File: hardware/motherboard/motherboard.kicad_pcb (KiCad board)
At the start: 6 copper layers, 32.4 x 32 mm, 2 parts, among them U201 STM32MP157AACx, U401 K4E6E304ED-EGCG

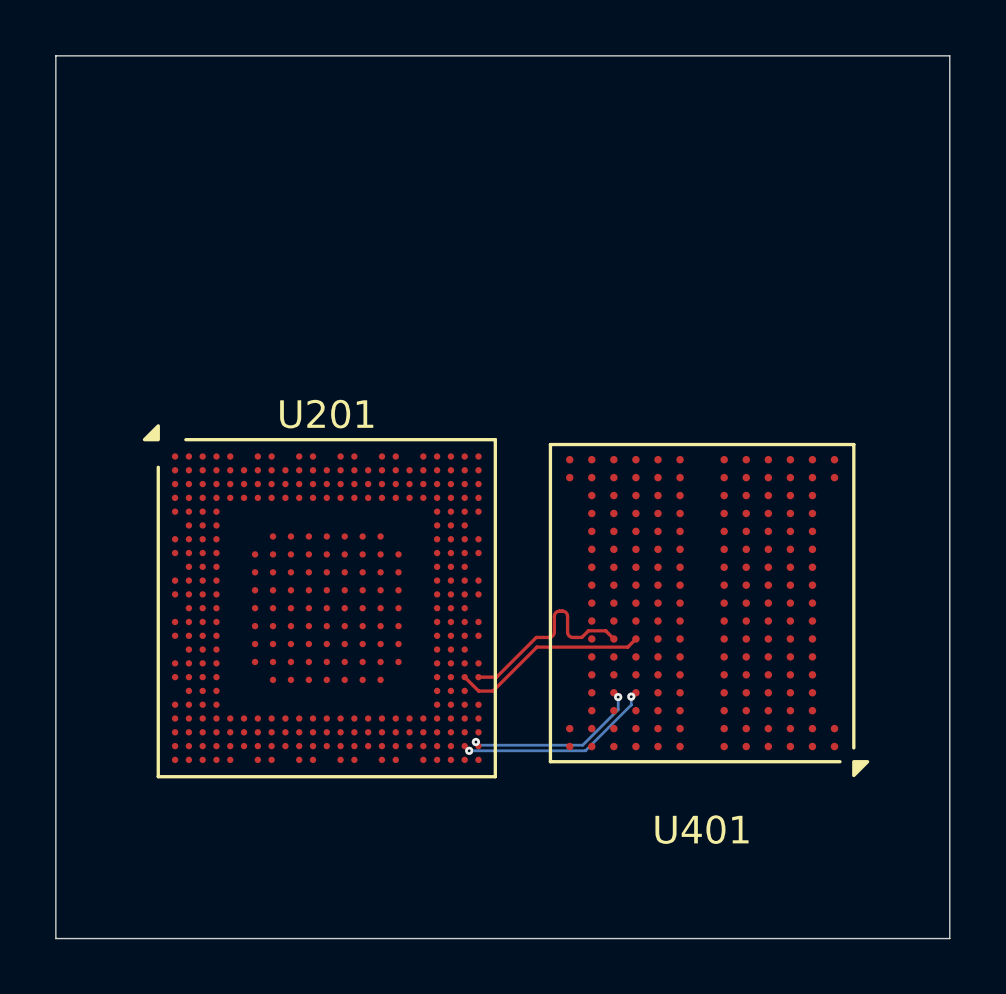
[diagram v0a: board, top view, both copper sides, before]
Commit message: Start routing RAM, add more docs
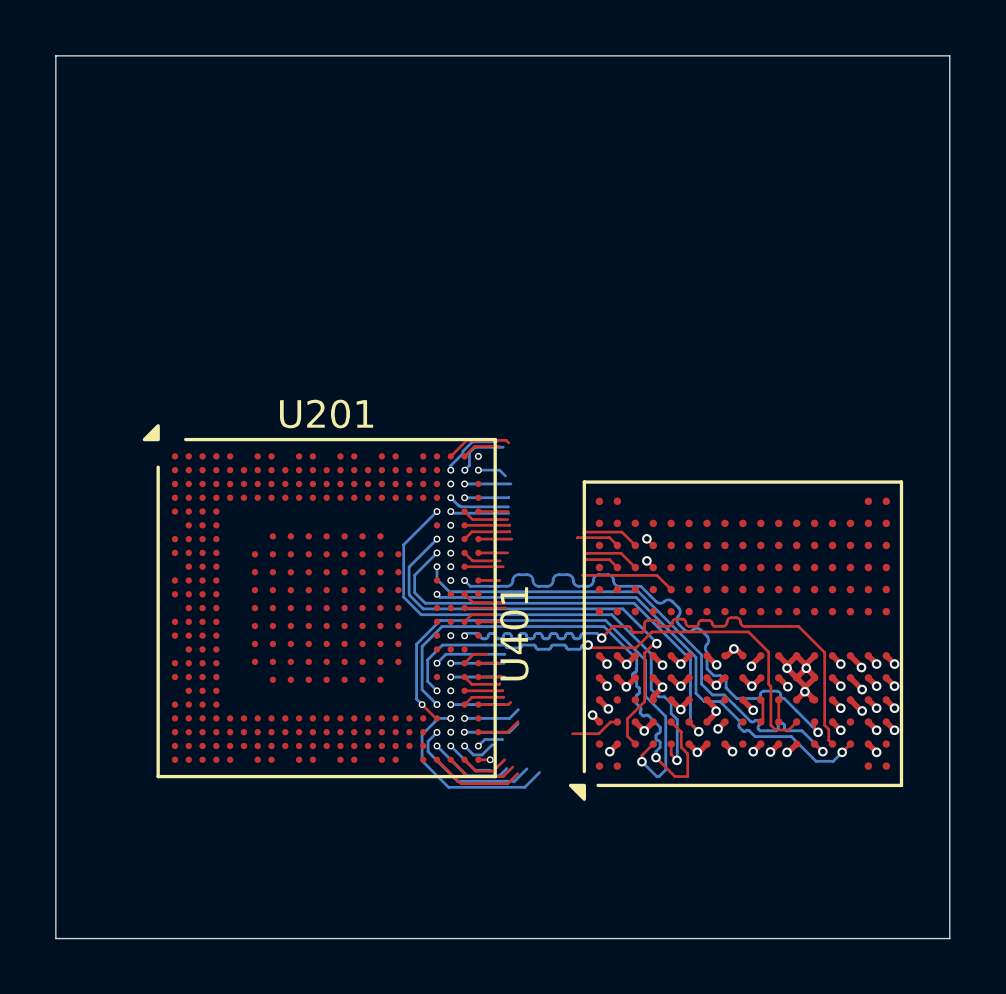
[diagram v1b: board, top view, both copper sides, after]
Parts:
- moved U401 1.85 mm to (151.3, 87.5), turned to 90 degrees
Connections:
- U401 pad A10: /RAM/VDD1 -> /CPU/PWR.VDD_{DDR}
- U401 pad A11: /RAM/VDDQ -> /CPU/PWR.VDD_{DDR}
- U401 pad A3: /RAM/VDD1 -> /CPU/PWR.VDD_{DDR}
- U401 pad A4: /RAM/VDD1 -> /CPU/PWR.VDD_{DDR}
- U401 pad A5: /RAM/VDD1 -> /CPU/PWR.VDD_{DDR}
- U401 pad A6: /RAM/VDD1 -> /CPU/PWR.VDD_{DDR}
- U401 pad A8: /RAM/VDD2 -> /CPU/PWR.VDD_{DDR}
- U401 pad A9: /RAM/VDD2 -> /CPU/PWR.VDD_{DDR}
- U401 pad C12: /RAM/VDDQ -> /CPU/PWR.VDD_{DDR}
- U401 pad D4: /RAM/VDD2 -> /CPU/PWR.VDD_{DDR}
- U401 pad D5: /RAM/VDD2 -> /CPU/PWR.VDD_{DDR}
- U401 pad D6: /RAM/VDD2 -> /CPU/PWR.VDD_{DDR}
- U401 pad E12: /RAM/VDDQ -> /CPU/PWR.VDD_{DDR}
- U401 pad E8: /RAM/VDDQ -> /CPU/PWR.VDD_{DDR}
- U401 pad F2: /RAM/VDDCA -> /CPU/PWR.VDD_{DDR}
- U401 pad G12: /RAM/VDDQ -> /CPU/PWR.VDD_{DDR}
- U401 pad G2: /RAM/VDDCA -> /CPU/PWR.VDD_{DDR}
- U401 pad G5: /RAM/VDD2 -> /CPU/PWR.VDD_{DDR}
- U401 pad H11: /RAM/VDDQ -> /CPU/PWR.VDD_{DDR}
- U401 pad H12: /RAM/VDD2 -> /CPU/PWR.VDD_{DDR}
- U401 pad H3: /RAM/VDDCA -> /CPU/PWR.VDD_{DDR}
- U401 pad H5: /RAM/VDD2 -> /CPU/PWR.VDD_{DDR}
- U401 pad H6: /RAM/VDD2 -> /CPU/PWR.VDD_{DDR}
- U401 pad H8: /RAM/VDDQ -> /CPU/PWR.VDD_{DDR}
- U401 pad H9: /RAM/VDDQ -> /CPU/PWR.VDD_{DDR}
- U401 pad J10: /RAM/VDDQ -> /CPU/PWR.VDD_{DDR}
- U401 pad J5: /RAM/VDD2 -> /CPU/PWR.VDD_{DDR}
- U401 pad J6: /RAM/VDD2 -> /CPU/PWR.VDD_{DDR}
- U401 pad J9: /RAM/VDDQ -> /CPU/PWR.VDD_{DDR}
- U401 pad K11: /RAM/VDDQ -> /CPU/PWR.VDD_{DDR}
- U401 pad K12: /RAM/VDD2 -> /CPU/PWR.VDD_{DDR}
- U401 pad K5: /RAM/VDD2 -> /CPU/PWR.VDD_{DDR}
- U401 pad K6: /RAM/VDD2 -> /CPU/PWR.VDD_{DDR}
- U401 pad K8: /RAM/VDDQ -> /CPU/PWR.VDD_{DDR}
- U401 pad L12: /RAM/VDDQ -> /CPU/PWR.VDD_{DDR}
- U401 pad L2: /RAM/VDDCA -> /CPU/PWR.VDD_{DDR}
- U401 pad L5: /RAM/VDD2 -> /CPU/PWR.VDD_{DDR}
- U401 pad M2: /RAM/VDDCA -> /CPU/PWR.VDD_{DDR}
- U401 pad N12: /RAM/VDDQ -> /CPU/PWR.VDD_{DDR}
- U401 pad N8: /RAM/VDDQ -> /CPU/PWR.VDD_{DDR}
- U401 pad P4: /RAM/VDD2 -> /CPU/PWR.VDD_{DDR}
- U401 pad P5: /RAM/VDD2 -> /CPU/PWR.VDD_{DDR}
- U401 pad P6: /RAM/VDD2 -> /CPU/PWR.VDD_{DDR}
- U401 pad R12: /RAM/VDDQ -> /CPU/PWR.VDD_{DDR}
- U401 pad U10: /RAM/VDD1 -> /CPU/PWR.VDD_{DDR}
- U401 pad U11: /RAM/VDDQ -> /CPU/PWR.VDD_{DDR}
- U401 pad U3: /RAM/VDD1 -> /CPU/PWR.VDD_{DDR}
- U401 pad U4: /RAM/VDD1 -> /CPU/PWR.VDD_{DDR}
- U401 pad U5: /RAM/VDD1 -> /CPU/PWR.VDD_{DDR}
- U401 pad U6: /RAM/VDD1 -> /CPU/PWR.VDD_{DDR}
- U401 pad U8: /RAM/VDD2 -> /CPU/PWR.VDD_{DDR}
- U401 pad U9: /RAM/VDD2 -> /CPU/PWR.VDD_{DDR}
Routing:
- net /CPU/DDR.A1: track 0.00 -> 20.1 mm, vias 0 -> 2
- net GND: track 0.00 -> 19.6 mm, vias 0 -> 32
- net /CPU/DDR.A6: track 0.00 -> 19.1 mm, vias 0 -> 2
- net /CPU/DDR.A0: track 0.00 -> 18.7 mm, vias 0 -> 2
- net /CPU/DDR.A2: track 0.00 -> 18.7 mm, vias 0 -> 2
- net /CPU/DDR.A4: track 0.00 -> 18.7 mm, vias 0 -> 2
- net /CPU/DDR.A8: track 0.00 -> 18.5 mm, vias 0 -> 2
- net /CPU/DDR.A3: track 0.00 -> 18.5 mm, vias 0 -> 2
- net /CPU/DDR.A7: track 0.00 -> 18.5 mm, vias 0 -> 2
- net /CPU/DDR.A9: track 0.00 -> 16.4 mm, vias 0 -> 2
- net /CPU/DDR.A5: track 0.00 -> 16.0 mm, vias 0 -> 2
- net /CPU/PWR.VDD_{DDR}: track 0.00 -> 11.9 mm, vias 0 -> 22
- net /CPU/DDR.DQ15: track 0.00 -> 7.12 mm, vias 0 -> 1
- net /CPU/DDR.DQS1-: track 7.28 -> 0.83 mm
- net /CPU/DDR.DQS1+: track 7.20 -> 1.40 mm
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- added copper zone on In2.Cu, net /CPU/PWR.VDD_{DDR}
- added copper zone on In1.Cu, net GND
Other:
- copper layers 6 -> 4

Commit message: Keep routing RAM
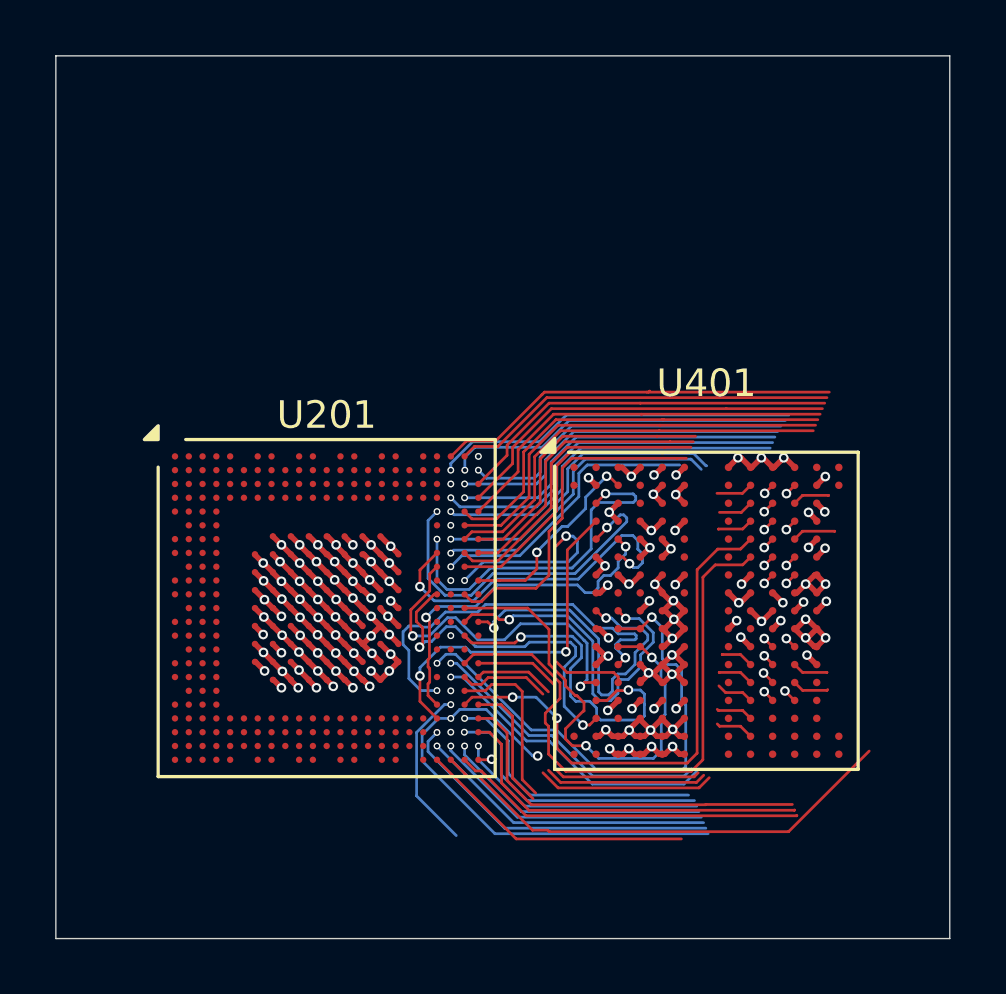
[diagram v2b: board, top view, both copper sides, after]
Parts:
- moved U401 1.56 mm to (150.0, 86.7), turned to 0 degrees
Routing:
- net GND: track 19.6 -> 55.6 mm, vias 32 -> 70
- net /CPU/PWR.VDD_{DDR}: track 11.9 -> 35.4 mm, vias 22 -> 38
- net /CPU/DDR.DQ10: track 0.96 -> 21.6 mm
- net /CPU/PWR.VDD_{CORE}: track 0.00 -> 15.2 mm, vias 0 -> 18
- net /CPU/DDR.CKE: track 3.45 -> 18.4 mm, vias 1 -> 2
- net /CPU/DDR.DQ0: track 1.68 -> 16.7 mm
- net /CPU/DDR.~{CS}: track 2.31 -> 17.1 mm, vias 0 -> 2
- net /CPU/DDR.DQ1: track 1.64 -> 16.4 mm
- net /CPU/DDR.DQ21: track 1.08 -> 15.7 mm
- net /CPU/DDR.DQ14: track 4.96 -> 19.4 mm, vias 0 -> 2
- net /CPU/DDR.DQ18: track 0.00 -> 14.2 mm
- net /CPU/DDR.DQ29: track 3.88 -> 17.9 mm, vias 0 -> 1
- net /CPU/DDR.DQM2: track 0.00 -> 14.0 mm
- net /CPU/DDR.DQS0+: track 1.75 -> 15.6 mm, vias 0 -> 1
- net /CPU/DDR.DQ30: track 1.60 -> 14.8 mm
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
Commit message: Rotate RAM IC, route data lanes partially
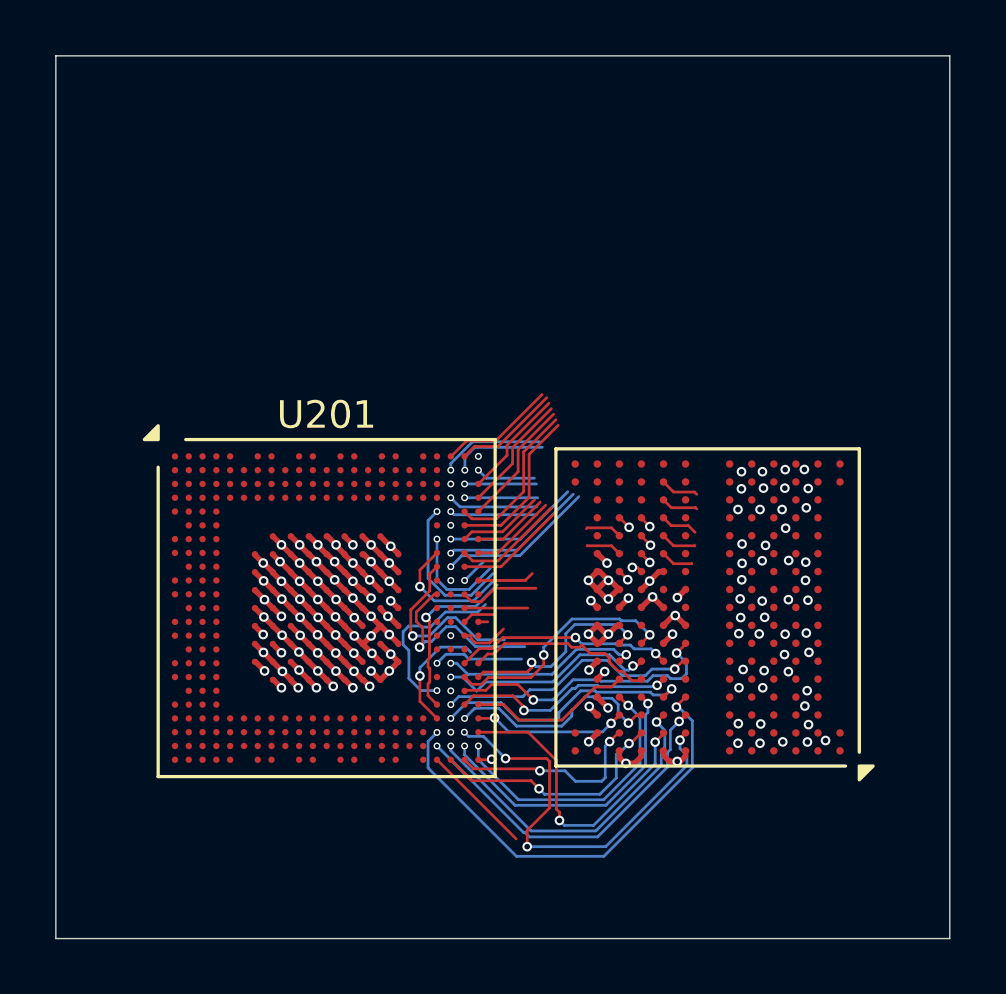
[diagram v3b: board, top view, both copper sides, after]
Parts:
- moved U401 0.13 mm to (150.0, 86.5), turned to 180 degrees
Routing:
- net GND: track 55.6 -> 33.5 mm, vias 70 -> 68
- net /CPU/PWR.VDD_{DDR}: track 35.4 -> 18.5 mm, vias 38 -> 37
- net /CPU/DDR.CKE: track 18.4 -> 3.27 mm
- net /CPU/DDR.~{CS}: track 17.1 -> 2.29 mm, vias 2 -> 1
- net /CPU/DDR.DQ10: track 21.6 -> 7.95 mm, vias 0 -> 2
- net /CPU/DDR.CLKN: track 12.8 -> 0.34 mm, vias 2 -> 1
- net /CPU/DDR.DQS0+: track 15.6 -> 3.53 mm
- net /CPU/DDR.A3: track 12.9 -> 0.95 mm, vias 2 -> 1
- net /CPU/DDR.CLKP: track 12.8 -> 1.18 mm, vias 2 -> 1
- net /CPU/DDR.DQ14: track 19.4 -> 8.15 mm
- net /CPU/DDR.A1: track 12.6 -> 1.79 mm, vias 2 -> 1
- net /CPU/DDR.DQ20: track 14.7 -> 4.24 mm
- net /CPU/DDR.DQ23: track 14.0 -> 3.86 mm
- net /CPU/DDR.DQS2-: track 12.7 -> 2.65 mm
- net /CPU/DDR.DQ22: track 13.2 -> 3.25 mm
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
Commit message: Add lpddr3 pcb layout rules, keep routing
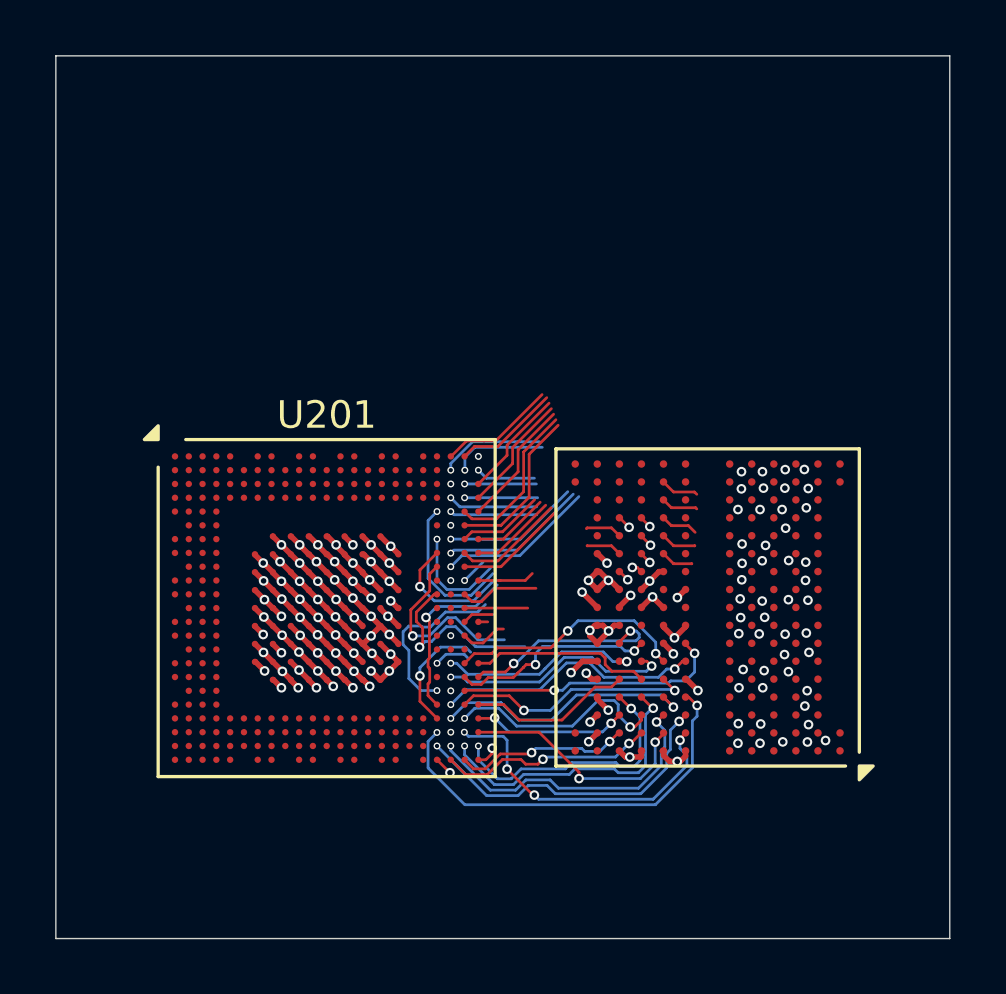
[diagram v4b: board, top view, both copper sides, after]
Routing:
- net /CPU/DDR.DQ31: track 15.3 -> 11.6 mm
- net /CPU/DDR.VREF: track 4.53 -> 1.36 mm, vias 1 -> 2
- net /CPU/DDR.DQ30: track 11.2 -> 8.72 mm
- net /CPU/DDR.CKE: track 3.27 -> 1.37 mm
- net /CPU/DDR.DQM3: track 16.6 -> 15.0 mm
- net GND: track 33.5 -> 35.1 mm
- net /CPU/DDR.DQS1+: track 8.85 -> 7.52 mm
- net /CPU/DDR.DQ27: track 12.9 -> 11.9 mm
- net /CPU/DDR.DQ26: track 12.1 -> 11.1 mm
- net /CPU/DDR.DQ28: track 7.34 -> 6.38 mm
- net /CPU/DDR.DQ29: track 8.85 -> 7.90 mm
- net /CPU/DDR.DQ10: track 7.95 -> 8.70 mm
- net /CPU/DDR.DQ14: track 8.15 -> 8.89 mm
- net /CPU/PWR.VDD_{DDR}: track 18.5 -> 17.9 mm
- net /CPU/DDR.DQS3-: track 10.2 -> 9.67 mm

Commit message: wip
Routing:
- net /CPU/DDR.A4: track 6.41 -> 28.6 mm
- net /CPU/DDR.CKE: track 1.37 -> 15.5 mm
- net /CPU/DDR.A6: track 6.49 -> 19.9 mm
- net /CPU/DDR.A8: track 4.32 -> 16.0 mm
- net /CPU/DDR.A5: track 4.75 -> 14.5 mm
- net /CPU/DDR.A1: track 1.73 -> 10.00 mm, vias 1 -> 2
- net /CPU/DDR.A2: track 6.86 -> 13.3 mm
- net /CPU/DDR.A7: track 5.49 -> 0.00 mm
- net /CPU/DDR.A0: track 6.85 -> 10.8 mm
- net /CPU/DDR.A9: track 3.87 -> 0.00 mm
- net /CPU/DDR.~{CS}: track 2.29 -> 4.91 mm
- net /CPU/DDR.DQS1-: track 7.54 -> 5.80 mm
- net /CPU/DDR.DQ31: track 11.6 -> 12.6 mm
- net /CPU/DDR.DQ9: track 8.45 -> 7.51 mm
- net /CPU/DDR.DQ14: track 8.89 -> 7.95 mm
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
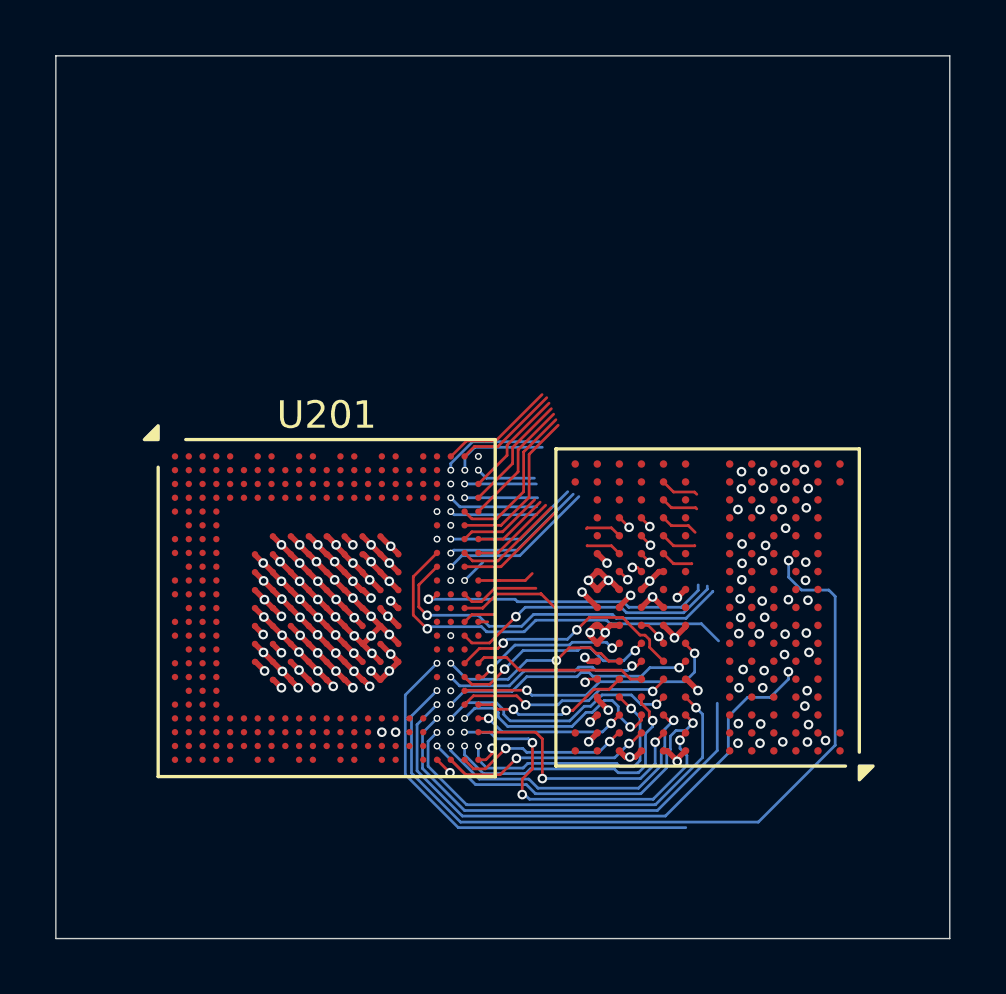
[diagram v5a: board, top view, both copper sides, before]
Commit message: ddr routing
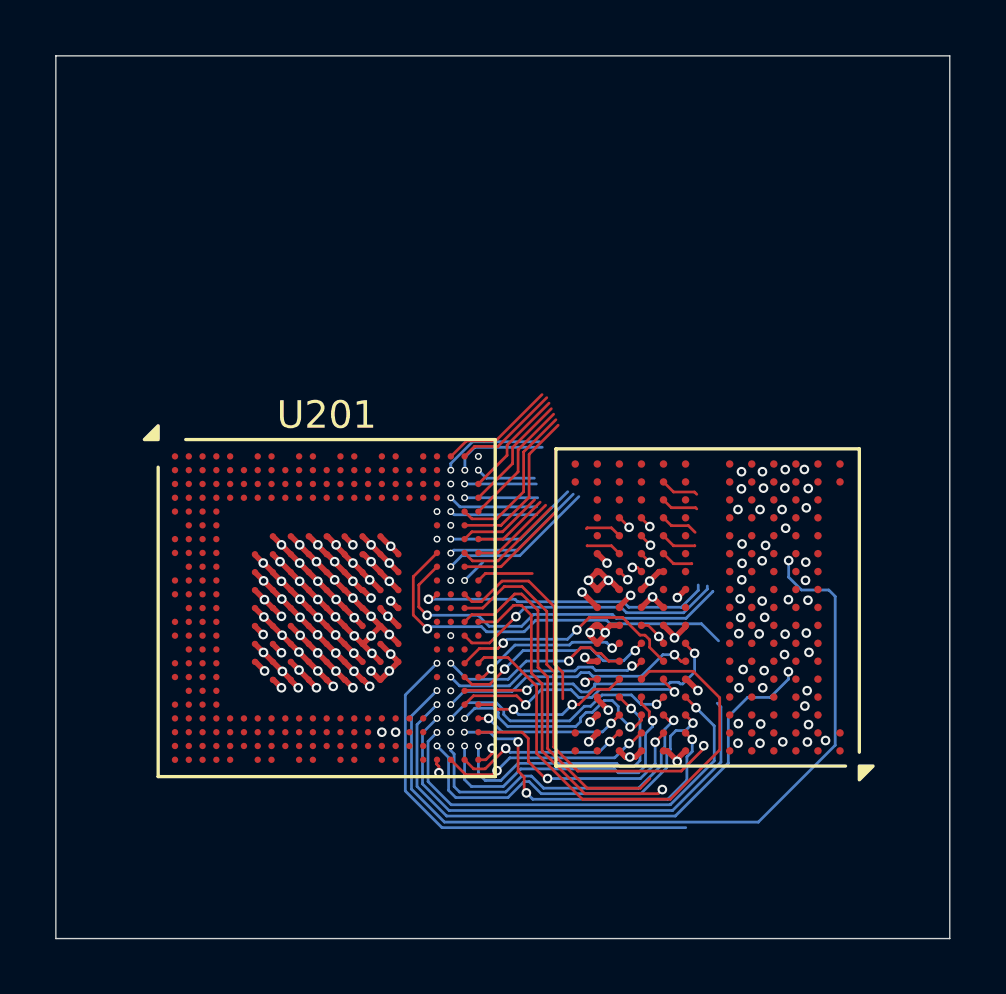
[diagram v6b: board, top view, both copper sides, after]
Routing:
- net /CPU/DDR.CLKN: track 0.34 -> 12.5 mm, vias 1 -> 2
- net /CPU/DDR.DQ13: track 6.34 -> 18.4 mm
- net /CPU/DDR.CLKP: track 1.18 -> 12.9 mm
- net /CPU/DDR.~{CS}: track 4.91 -> 15.0 mm, vias 1 -> 2
- net /CPU/DDR.ODT: track 2.90 -> 7.53 mm
- net /CPU/DDR.DQ27: track 12.1 -> 13.2 mm
- net /CPU/DDR.DQ26: track 11.0 -> 12.1 mm
- net /CPU/DDR.DQ14: track 7.95 -> 9.01 mm
- net /CPU/DDR.DQM3: track 15.0 -> 16.0 mm
- net /CPU/DDR.DQS3+: track 10.2 -> 11.1 mm
- net /CPU/DDR.A8: track 16.0 -> 16.7 mm
- net /CPU/DDR.DQS3-: track 9.32 -> 9.99 mm
- net /CPU/DDR.A6: track 19.9 -> 20.5 mm
